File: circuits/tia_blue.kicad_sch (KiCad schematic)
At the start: 11 parts, among them U4 OPA380AID

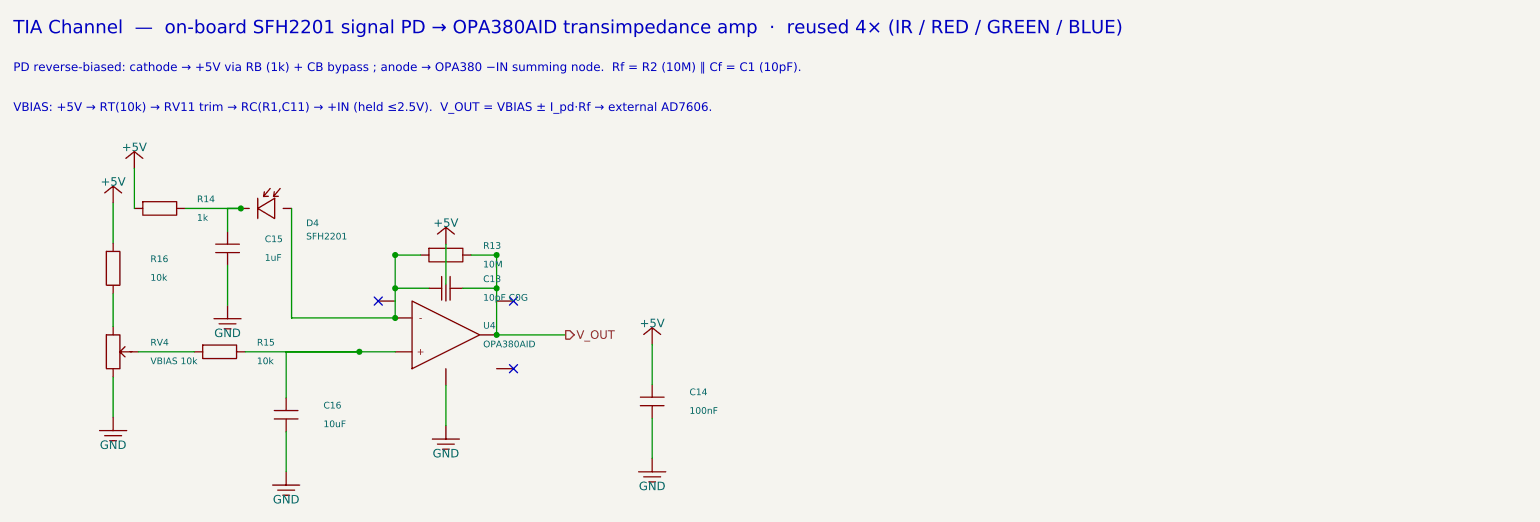
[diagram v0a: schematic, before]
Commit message: fix(circuits): import mcu sheet and laser footprints
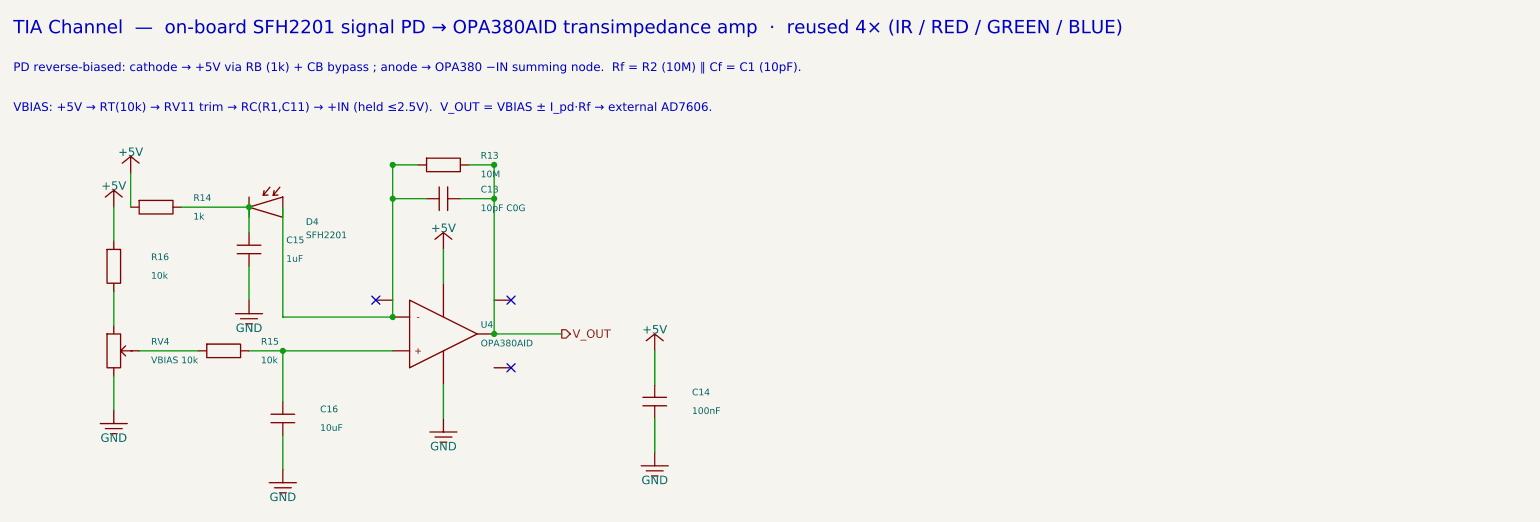
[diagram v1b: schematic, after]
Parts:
- removed C14: 100nF, Capacitor_SMD:C_0402_1005Metric_Pad0.74x0.62mm_HandSolder, symbol viv:C_V
- removed C15: 1uF, Capacitor_SMD:C_0402_1005Metric_Pad0.74x0.62mm_HandSolder, symbol viv:C_V
- removed R16: 10k, Resistor_SMD:R_0603_1608Metric_Pad0.98x0.95mm_HandSolder, symbol viv:R_V
- removed RV4: VBIAS 10k, Potentiometer_SMD:Potentiometer_Bourns_3224W_Vertical, symbol viv:POT_V
- removed U4: OPA380AID, Package_SO:SOIC-8_3.9x4.9mm_P1.27mm, symbol viv:OPA_N
- added C13: 10pF C0G, Capacitor_SMD:C_0603_1608Metric_Pad1.08x0.95mm_HandSolder, symbol viv:C_H
- added D4: SFH2201, OptoDevice:Osram_SFH2201, symbol viv:PHOTODIODE
- added R13: 10M, Resistor_SMD:R_0603_1608Metric_Pad0.98x0.95mm_HandSolder, symbol viv:R_H
- added R14: 1k, Resistor_SMD:R_0603_1608Metric_Pad0.98x0.95mm_HandSolder, symbol viv:R_H
- added R15: 10k, Resistor_SMD:R_0603_1608Metric_Pad0.98x0.95mm_HandSolder, symbol viv:R_H
- C14: renamed from R15; value 10k -> 100nF; footprint Resistor_SMD:R_0603_1608Metric_Pad0.98x0.95mm_HandSolder -> Capacitor_SMD:C_0402_1005Metric_Pad0.74x0.62mm_HandSolder; symbol viv:R_H -> viv:C_V; LCSC C269701 -> C83056; Part Number 0603WAF1002T5E -> 0402B104K160CT
- C15: renamed from D4; value SFH2201 -> 1uF; footprint OptoDevice:Osram_SFH2201 -> Capacitor_SMD:C_0402_1005Metric_Pad0.74x0.62mm_HandSolder; symbol viv:PHOTODIODE -> viv:C_V; LCSC C2900216 -> C7472946; Part Number SFH2201 -> HGC0402R5105K250NTEJ
- C16: LCSC C15850 -> C318691; Part Number CL21A106KAYNNNE -> CL21A106KAYNNNG
- R16: renamed from R13; value 10M -> 10k; symbol viv:R_H -> viv:R_V; LCSC C57129 -> C844918; Part Number 0603WAF1005T5E -> CRCW060310K0FKEA
- RV4: renamed from C13; value 10pF C0G -> VBIAS 10k; footprint Capacitor_SMD:C_0603_1608Metric_Pad1.08x0.95mm_HandSolder -> Potentiometer_SMD:Potentiometer_Bourns_3224W_Vertical; symbol viv:C_H -> viv:POT_V; LCSC C106245 -> C81348; Part Number CC0603JRNPO9BN100 -> 3224W-1-103E
- U4: renamed from R14; value 1k -> OPA380AID; footprint Resistor_SMD:R_0603_1608Metric_Pad0.98x0.95mm_HandSolder -> Package_SO:SOIC-8_3.9x4.9mm_P1.27mm; symbol viv:R_H -> viv:OPA_N; LCSC C21190 -> C201677; Part Number 0603WAF1001T5E -> OPA380AID
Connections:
- net +5V: now also C14.1, R16.1, U4.7 (V+), R14.1; no longer U4.1
- net GND: now also C14.2, C15.2, RV4.3, U4.4 (V-)
- net V_OUT: now also U4.6, C13.2, R13.2; no longer R16.2, RV4.2
- net at C15.1: now also D4.1 (K), R14.2; no longer U4.2
- net at C16.1: now also U4.3 (+), R15.2; no longer C14.2
- new net: C13.1, D4.2 (A), R13.1, U4.2 (-)
- new net: R16.2, RV4.1
- new net: R15.1, RV4.2 (W)
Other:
- moved on the sheet: R16

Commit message: save laser controller schematic and layout state
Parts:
- removed C13: 10pF C0G, Capacitor_SMD:C_0603_1608Metric_Pad1.08x0.95mm_HandSolder, symbol viv:C_H
- removed D4: SFH2201, OptoDevice:Osram_SFH2201, symbol viv:PHOTODIODE
- removed R16: 10k, Resistor_SMD:R_0603_1608Metric_Pad0.98x0.95mm_HandSolder, symbol viv:R_V
- added C14: 100nF, Capacitor_SMD:C_0402_1005Metric_Pad0.74x0.62mm_HandSolder, symbol viv:C_V
- added C16: 10uF, Capacitor_SMD:C_0805_2012Metric_Pad1.18x1.45mm_HandSolder, symbol viv:C_V
- added R15: 10k, Resistor_SMD:R_0603_1608Metric_Pad0.98x0.95mm_HandSolder, symbol viv:R_H
- C13: renamed from R15; value 10k -> 10pF C0G; footprint Resistor_SMD:R_0603_1608Metric_Pad0.98x0.95mm_HandSolder -> Capacitor_SMD:C_0603_1608Metric_Pad1.08x0.95mm_HandSolder; symbol viv:R_H -> viv:C_H; LCSC C844918 -> C106245; Part Number CRCW060310K0FKEA -> CC0603JRNPO9BN100
- D4: renamed from U4; value OPA380AID -> SFH2201; footprint Package_SO:SOIC-8_3.9x4.9mm_P1.27mm -> OptoDevice:Osram_SFH2201; symbol viv:OPA_N -> viv:PHOTODIODE; LCSC C201677 -> C2900216; Part Number OPA380AID -> SFH2201
- R16: renamed from C16; value 10uF -> 10k; footprint Capacitor_SMD:C_0805_2012Metric_Pad1.18x1.45mm_HandSolder -> Resistor_SMD:R_0603_1608Metric_Pad0.98x0.95mm_HandSolder; symbol viv:C_V -> viv:R_V; LCSC C318691 -> C844918; Part Number CL21A106KAYNNNG -> CRCW060310K0FKEA
- RV4: renamed from C14; value 100nF -> VBIAS 10k; footprint Capacitor_SMD:C_0402_1005Metric_Pad0.74x0.62mm_HandSolder -> Potentiometer_SMD:Potentiometer_Bourns_3224W_Vertical; symbol viv:C_V -> viv:POT_V; LCSC C83056 -> C81348; Part Number 0402B104K160CT -> 3224W-1-103E
- RV8: renamed from RV4; value VBIAS 10k -> RF 2M; symbol viv:POT_V -> viv:POT_H; LCSC C81348 -> C116323; Part Number 3224W-1-103E -> 3224W-1-205E
- U4: renamed from R13; value 10M -> OPA380AID; footprint Resistor_SMD:R_0603_1608Metric_Pad0.98x0.95mm_HandSolder -> Package_SO:SOIC-8_3.9x4.9mm_P1.27mm; symbol viv:R_H -> viv:OPA_N; LCSC C844730 -> C201677; Part Number CRCW060310M0FKEA -> OPA380AID
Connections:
- net +5V: now also R16.1, U4.7 (V+), C14.1; no longer D4.7 (V+), RV4.1
- net GND: now also RV4.3, U4.4 (V-), C14.2, C16.2; no longer D4.4 (V-), R16.2, RV4.2, RV8.3
- net V_OUT: now also C13.2, RV8.2 (W), RV8.3, U4.6; no longer D4.6, U4.2
- net at C15.1, R14.2: now also D4.1 (K)
- net at D4.2 (A): now also C13.1, RV8.1, U4.2 (-); no longer U4.1
- new net: C16.1, R15.2, U4.3 (+)
- new net: R16.2, RV4.1
- new net: R15.1, RV4.2 (W)
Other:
- note added: "PD reverse-biased: cathode → +5V via RB (1k) + CB bypass ; anode → OPA380 −IN summing node. Rf = RVFB (2M trim) ∥ Cf = C1 (10pF)."
- note added: "VBIAS: +5V → RT(10k) → RV11 trim → RC(R1,C11) → +IN (held ≤2.5V). V_OUT = VBIAS ± I_pd·Rf → on-board AD7606-4."
- note removed: "PD reverse-biased: cathode → +5V via RB (1k) + CB bypass ; anode → OPA380 −IN summing node. Rf = R2 (10M) ∥ Cf = C1 (10pF)."
- note removed: "VBIAS: +5V → RT(10k) → RV11 trim → RC(R1,C11) → +IN (held ≤2.5V). V_OUT = VBIAS ± I_pd·Rf → external AD7606."
- moved on the sheet: RV8
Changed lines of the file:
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@@
     )
   )
-  (symbol (lib_id "viv:R_H") (at 214.63 124.46 0) (unit 1)
-    (in_bom yes) (on_board yes) (dnp no)
-    (property "Reference" "R13" (at 220.23 123.06 0) (effects (font (size 1.0 1.0)) (justify left)))
-    (property "Value" "10M" (at 220.23 125.86 0) (effects (font (size 1.0 1.0)) (justify left)))
-    (property "Footprint" "Resistor_SMD:R_0603_1608Metric_Pad0.98x0.95mm_HandSolder" (at 214.63 124.46 0) (effects (font (size 1.0 1.0)) hide))
+  (symbol (lib_id "viv:POT_H") (at 214.63 124.46 0) (unit 1)
+    (in_bom yes) (on_board yes) (dnp no)
+    (property "Reference" "RV8" (at 220.23 123.06 0) (effects (font (size 1.0 1.0)) (justify left)))
+    (property "Value" "RF 2M" (at 220.23 125.86 0) (effects (font (size 1.0 1.0)) (justify left)))
+    (property "Footprint" "Potentiometer_SMD:Potentiometer_Bourns_3224W_Vertical" (at 214.63 124.46 0) (effects (font (size 1.0 1.0)) hide))
     (property "Datasheet" "" (at 214.63 124.46 0) (effects (font (size 1.0 1.0)) hide))
-    (property "Part Number" "CRCW060310M0FKEA" (at 214.63 124.46 0) (effects (font (size 1.0 1.0)) hide))
-    (property "LCSC" "C844730" (at 214.63 124.46 0) (effects (font (size 1.0 1.0)) hide))
-    (pin "1")
-    (pin "2")
-    (instances
-      (project "laser_controller"
-        (path "/c1d2e3f4-6000-4000-a000-000000000001" (reference "R13") (unit 1))
+    (property "Part Number" "3224W-1-205E" (at 214.63 124.46 0) (effects (font (size 1.0 1.0)) hide))
+    (property "LCSC" "C116323" (at 214.63 124.46 0) (effects (font (size 1.0 1.0)) hide))
+    (pin "1")
+    (pin "2")
+    (pin "3")
+    (instances
+      (project "laser_controller"
+        (path "/c1d2e3f4-6000-4000-a000-000000000001" (reference "RV8") (unit 1))
       )
     )
@@
   (wire (pts (xy 210.82 124.46) (xy 207.01 124.46)) (stroke (width 0) (type default)))
   (wire (pts (xy 218.44 124.46) (xy 222.25 124.46)) (stroke (width 0) (type default)))
+  (wire (pts (xy 214.63 120.65) (xy 222.25 120.65)) (stroke (width 0) (type default)))
+  (wire (pts (xy 222.25 120.65) (xy 222.25 124.46)) (stroke (width 0) (type default)))
   (wire (pts (xy 212.09 129.54) (xy 207.01 129.54)) (stroke (width 0) (type default)))
   (wire (pts (xy 217.17 129.54) (xy 222.25 129.54)) (stroke (width 0) (type default)))
@@
   (hierarchical_label "V_OUT" (shape output) (at 232.41 149.86 0) (effects (font (size 1.27 1.27)) (justify left)))
   (text "TIA Channel  —  on-board SFH2201 signal PD → OPA380AID transimpedance amp  ·  reused 4× (IR / RED / GREEN / BLUE)" (at 150 104 0) (effects (font (size 2.0 2.0)) (justify left)))
-  (text "PD reverse-biased: cathode → +5V via RB (1k) + CB bypass ; anode → OPA380 −IN summing node.  Rf = R2 (10M) ∥ Cf = C1 (10pF)." (at 150 110 0) (effects (font (size 1.3 1.3)) (justify left)))
-  (text "VBIAS: +5V → RT(10k) → RV11 trim → RC(R1,C11) → +IN (held ≤2.5V).  V_OUT = VBIAS ± I_pd·Rf → external AD7606." (at 150 116 0) (effects (font (size 1.3 1.3)) (justify left)))
+  (text "PD reverse-biased: cathode → +5V via RB (1k) + CB bypass ; anode → OPA380 −IN summing node.  Rf = RVFB (2M trim) ∥ Cf = C1 (10pF)." (at 150 110 0) (effects (font (size 1.3 1.3)) (justify left)))
+  (text "VBIAS: +5V → RT(10k) → RV11 trim → RC(R1,C11) → +IN (held ≤2.5V).  V_OUT = VBIAS ± I_pd·Rf → on-board AD7606-4." (at 150 116 0) (effects (font (size 1.3 1.3)) (justify left)))
   (sheet_instances
     (path "/" (page "1"))
